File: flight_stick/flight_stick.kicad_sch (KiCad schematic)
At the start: 80 parts, among them J1 Load Cell 1, J10 USB_C_Receptacle_USB2.0, J11 Conn_01x05_Pin, J2 Load Cell 2, J3 Load Cell 5, J4 Load Cell 6, J5 Load Cell 3, J6 Load Cell 4, J7 Conn_01x04_Male, J8 Conn_01x05_Pin, J9 Conn_01x04_Male, Q1 MMS8550, Q2 MMS8550, Q3 MMS8550, Q4 2N7002, Q5 2N7002, Q6 2N7002, Q7 2N7002, Q8 2N7002, SW1 SW_Push, U1 HX711, U2 HX711, U3 HX711, U4 STM32F103C8Tx, U5 AZ1117-3.3, Y1 8Mhz

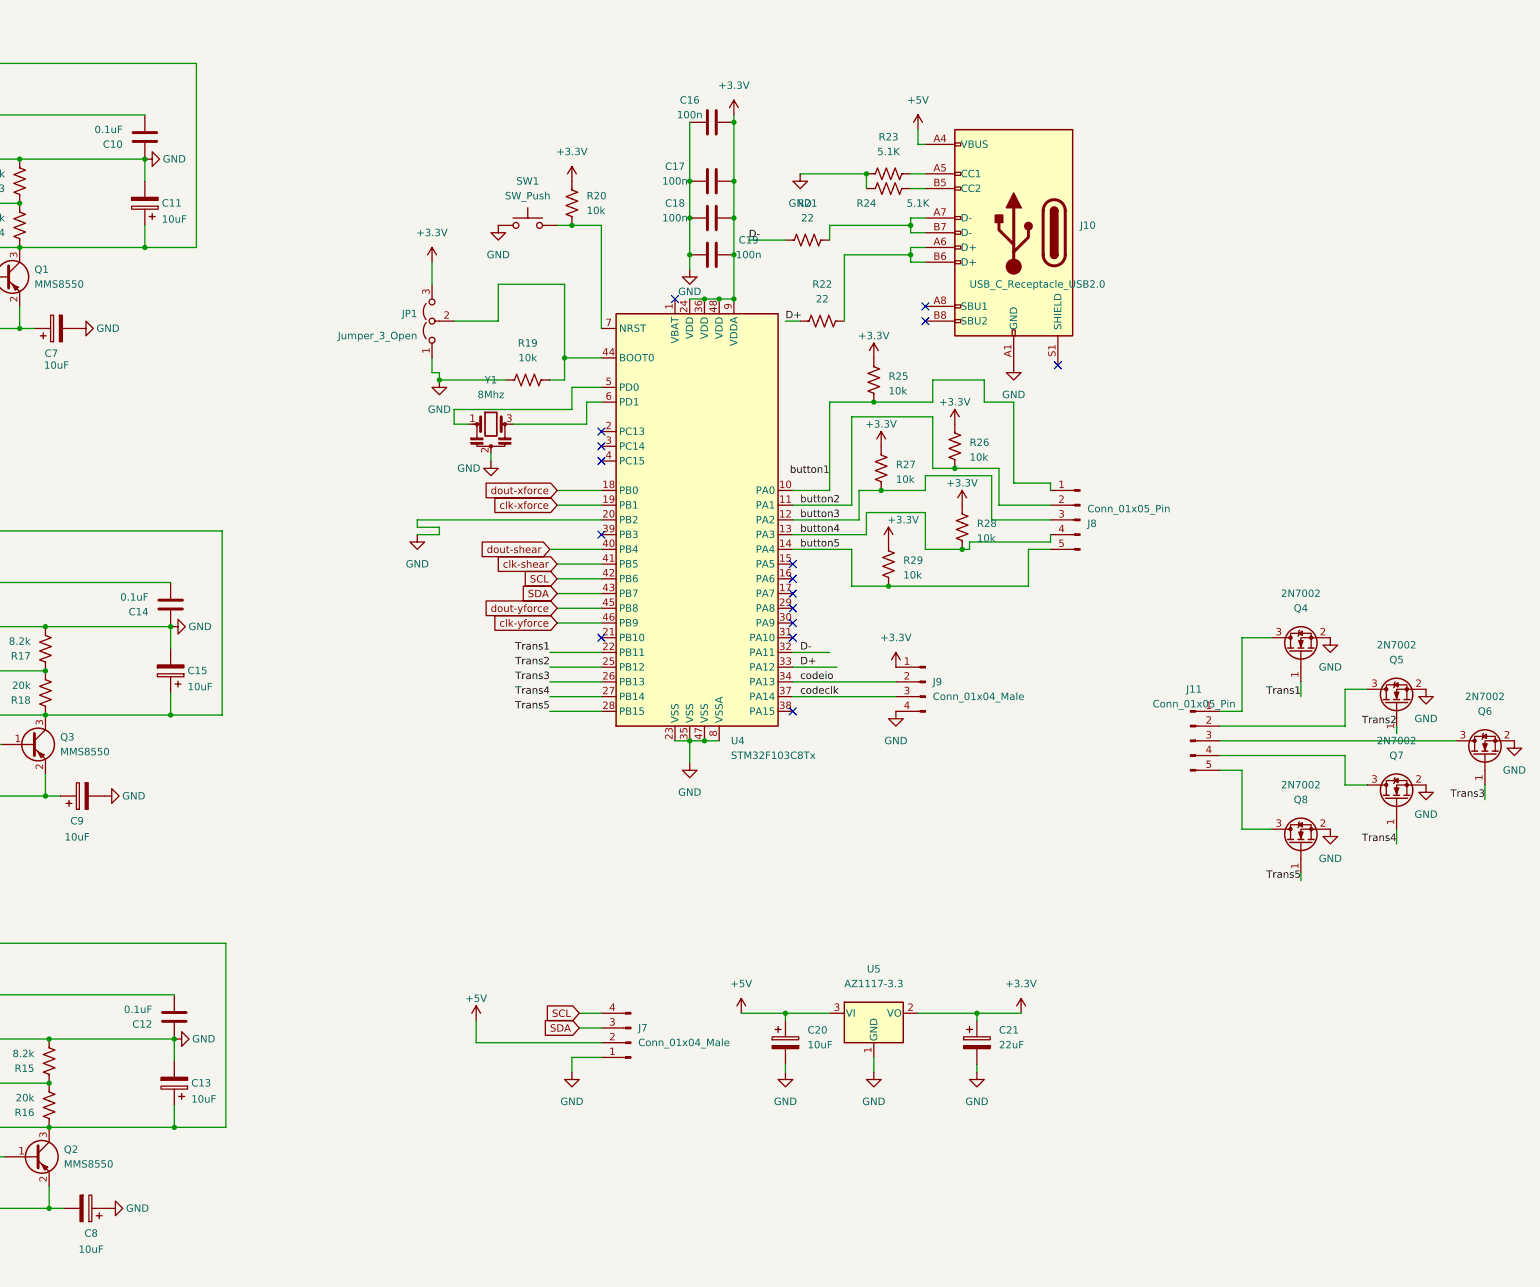
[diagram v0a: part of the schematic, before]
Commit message: Added extra LEDs, replaced Voltage reg., added redundant SW, reviewed USB placement
Added many new features
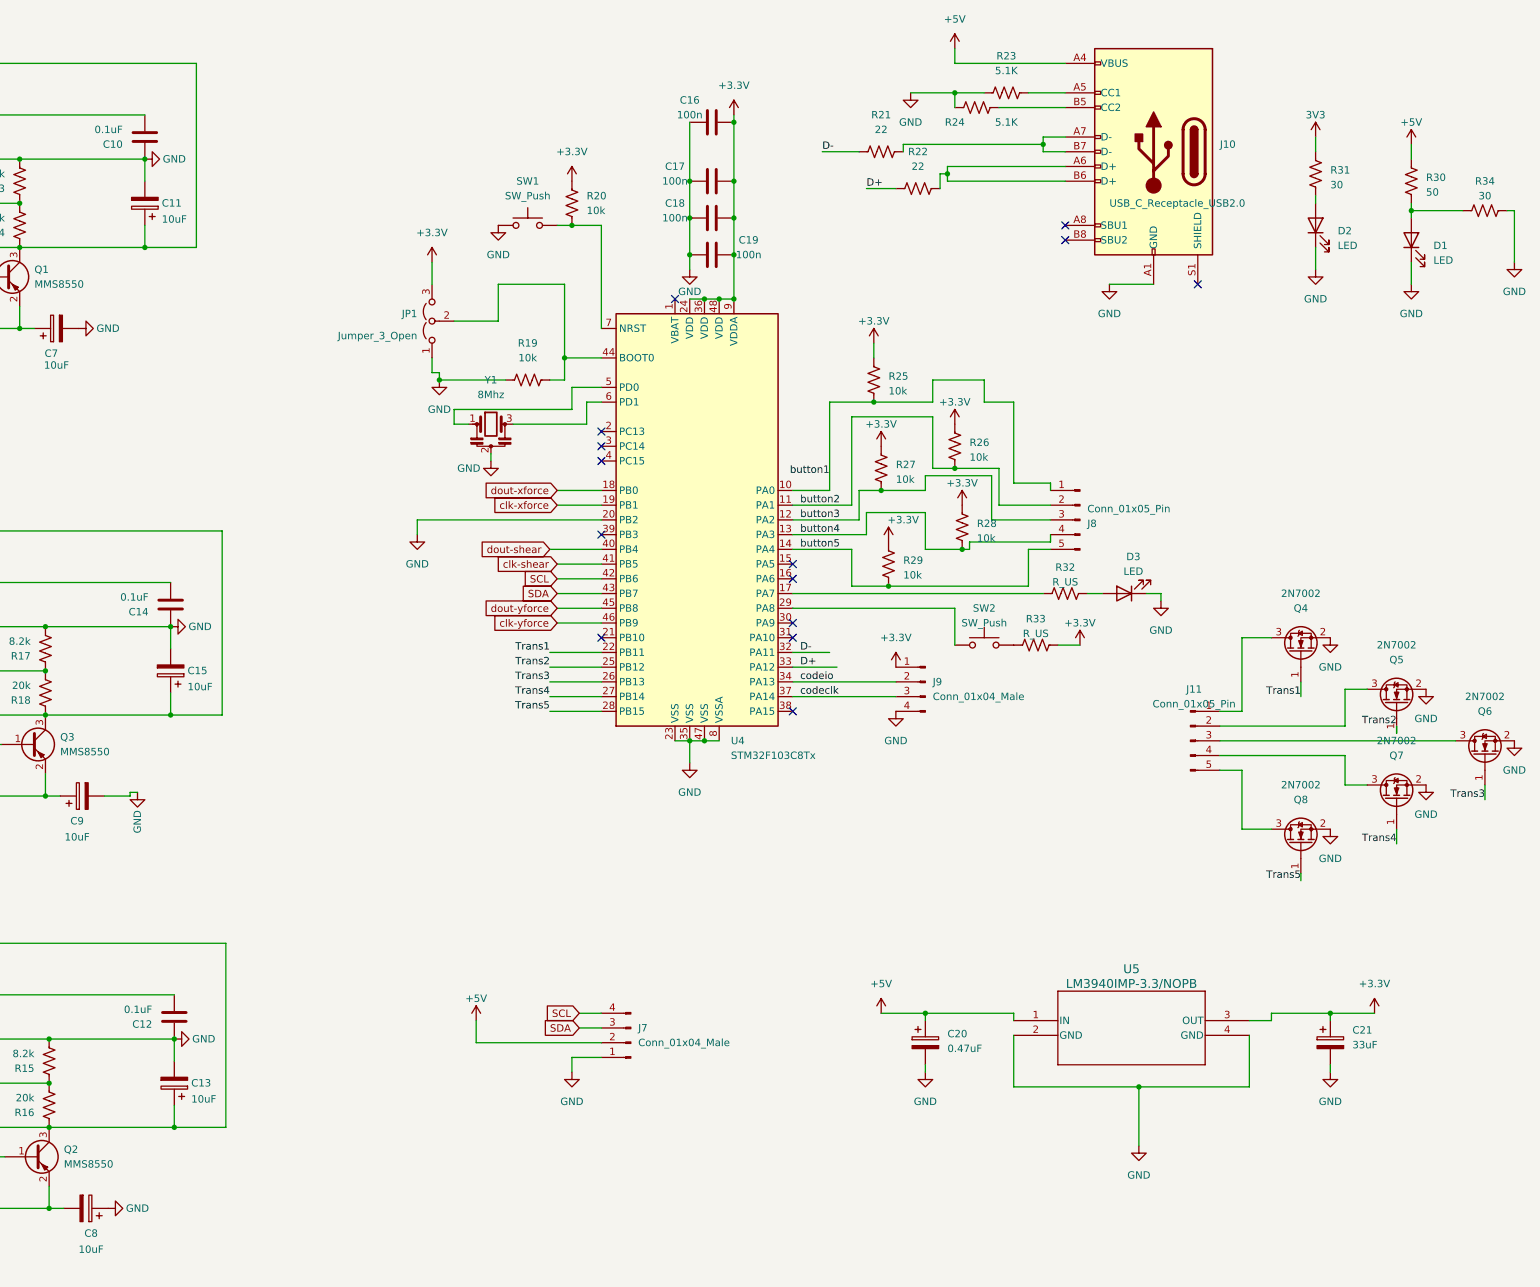
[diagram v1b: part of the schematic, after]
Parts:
- removed U5: AZ1117-3.3, Package_TO_SOT_SMD:SOT-223-3_TabPin2, symbol Regulator_Linear:AZ1117-3.3
- added D1, D2, D3: LED, LED_SMD:LED_2010_5025Metric, symbol Device:LED
- added R30: 50, Resistor_SMD:R_0603_1608Metric, symbol Device:R_US
- added R31: 30, Resistor_SMD:R_0603_1608Metric, symbol Device:R_US
- added R32, R33: R_US, Resistor_SMD:R_0603_1608Metric, symbol Device:R_US
- added R34: 30, symbol Device:R_US
- added SW2: SW_Push, symbol Switch:SW_Push
- added U5: LM3940IMP-3.3/NOPB, MP04A, symbol 2024-03-22_01-04-52:LM3940IMP-3.3_NOPB
- C20: value 10uF -> 0.47uF
- C21: value 22uF -> 33uF
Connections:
- net +3.3V: now also R33.2, U5.3 (OUT)
- net +5V: now also R30.1, R31.1, U5.1 (IN)
- net GND: now also D1.1 (K), D2.1 (K), D3.1 (K), R34.2, U5.2 (GND), U5.4 (GND)
- net at U4.17 (PA7): now also R32.1
- net at U4.29 (PA8): now also SW2.1
- new net: R33.1, SW2.2
- new net: D1.2 (A), R30.2, R34.1
- new net: D3.2 (A), R32.2
- new net: D2.2 (A), R31.2
- no-connect marks 19 -> 17
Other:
- moved on the sheet: C20, C21, J10, R21, R22, R23, R24

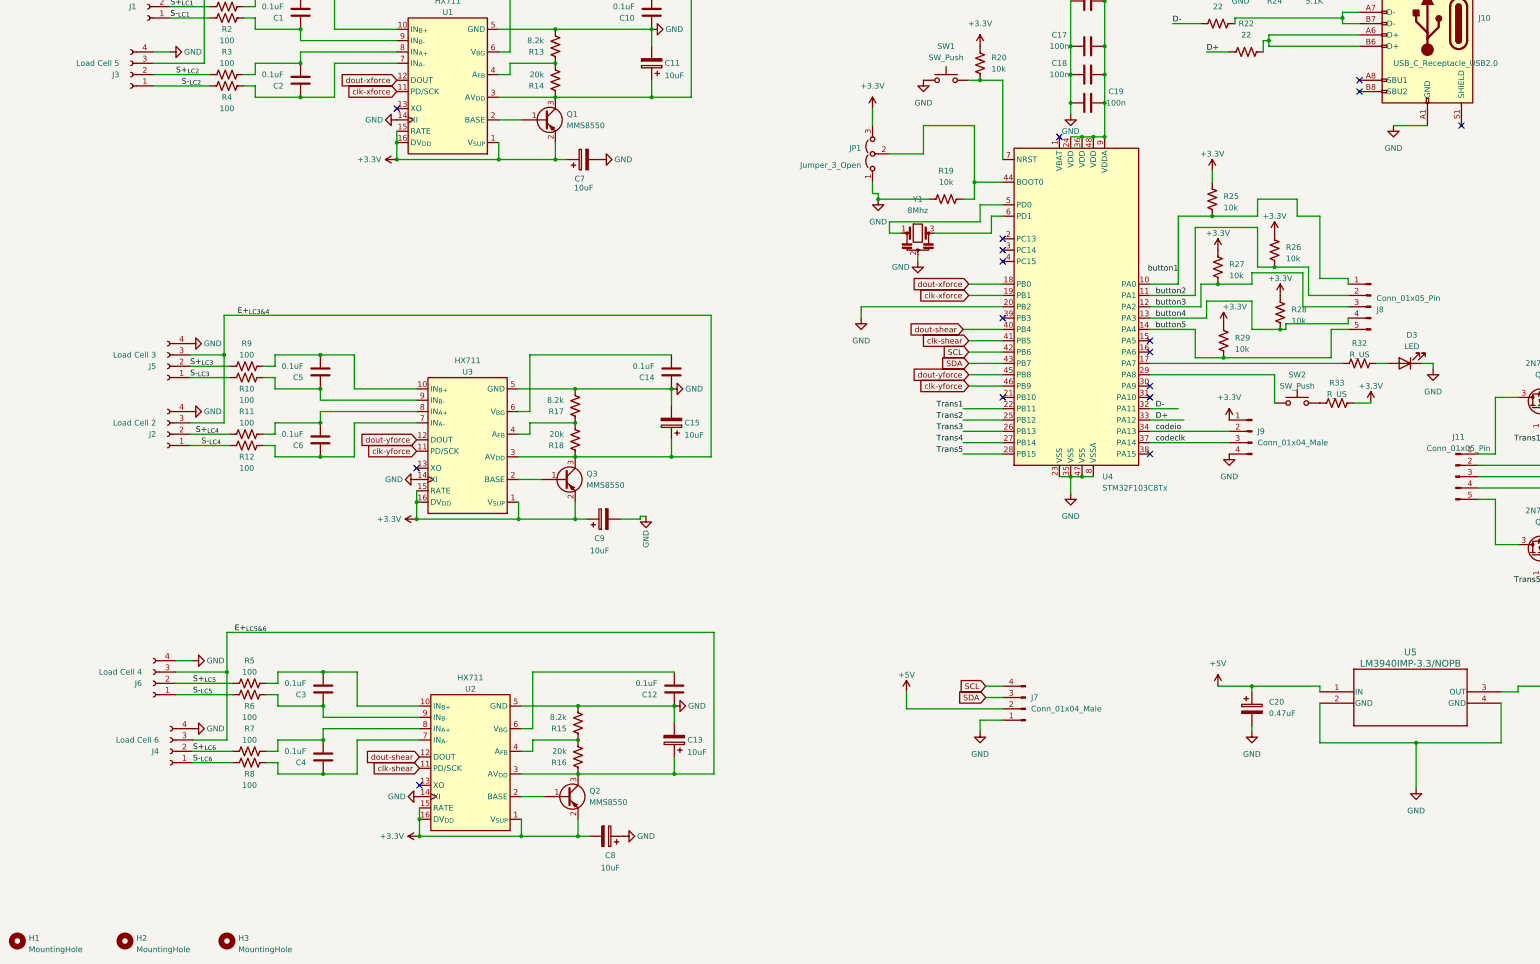
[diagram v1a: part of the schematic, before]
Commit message: updated 3rd revision
reduced the number of strain gauges and updated the schematic and placed the initial layout without traces.
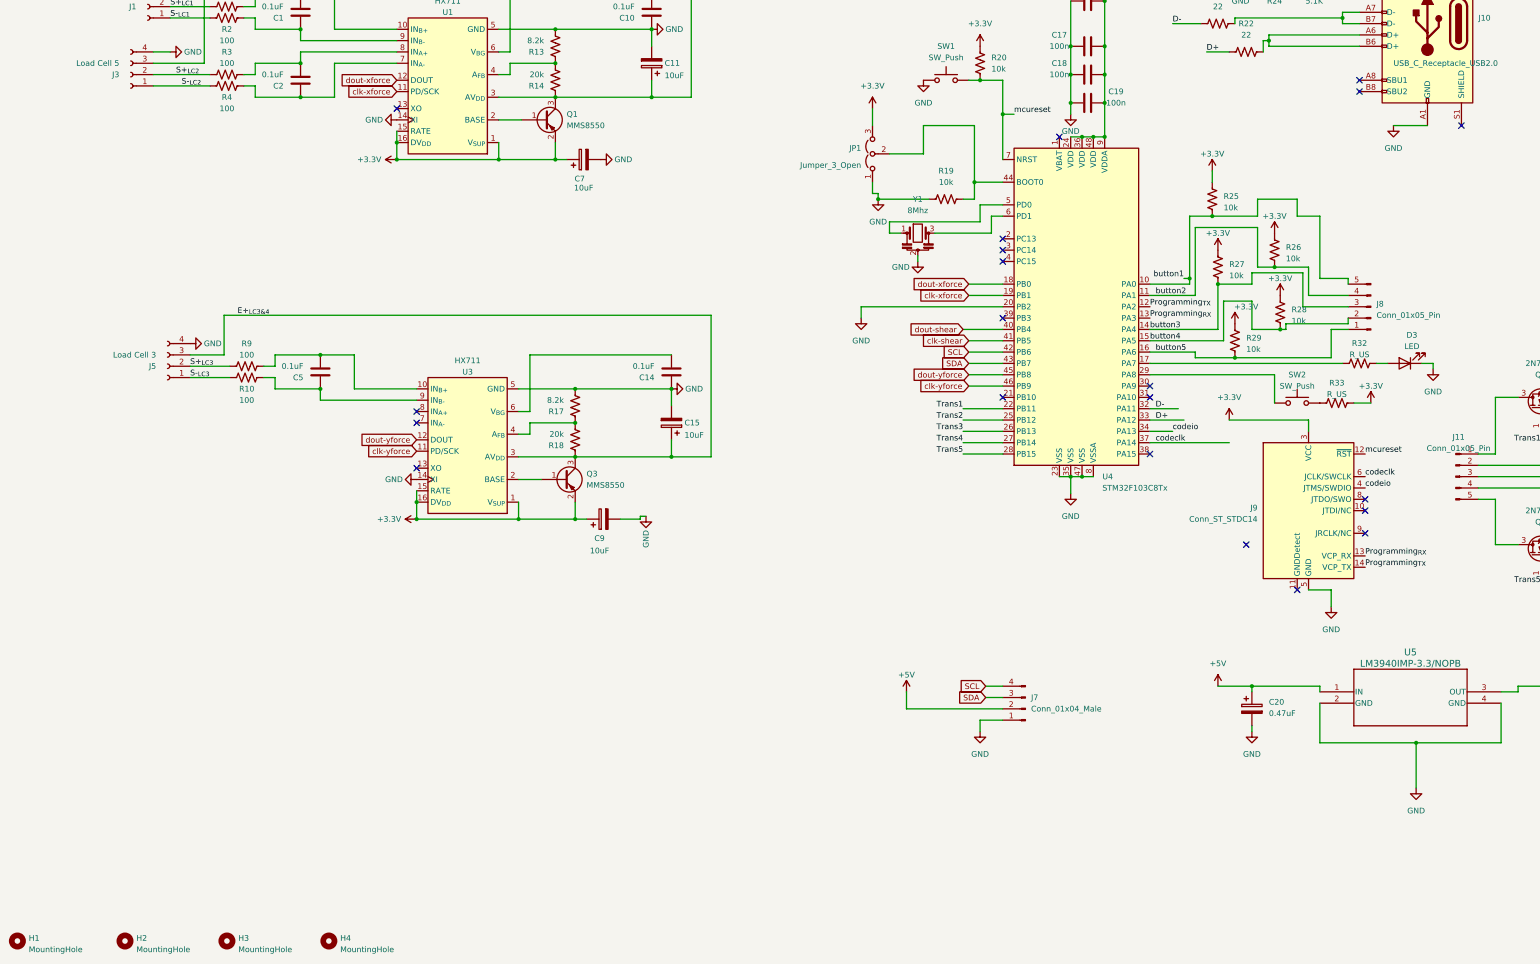
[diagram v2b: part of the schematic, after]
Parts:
- removed C12, C3, C4, C6: 0.1uF, Capacitor_SMD:C_0603_1608Metric, symbol Device:C
- removed C13, C8: 10uF, Capacitor_SMD:C_0603_1608Metric, symbol Device:C_Polarized
- removed J2: Load Cell 2, Connector_PinHeader_2.54mm:PinHeader_1x04_P2.54mm_Vertical, symbol Connector:Conn_01x04_Female
- removed J4: Load Cell 6, Connector_PinHeader_2.54mm:PinHeader_1x04_P2.54mm_Vertical, symbol Connector:Conn_01x04_Female
- removed J6: Load Cell 4, Connector_PinHeader_2.54mm:PinHeader_1x04_P2.54mm_Vertical, symbol Connector:Conn_01x04_Female
- removed J9: Conn_01x04_Male, Connector_PinHeader_2.54mm:PinHeader_1x04_P2.54mm_Horizontal, symbol Connector:Conn_01x04_Male
- removed Q2: MMS8550, Package_TO_SOT_SMD:SOT-23, symbol Device:Q_PNP_BEC
- removed R11, R12, R5, R6, R7, R8: 100, Resistor_SMD:R_0603_1608Metric, symbol Device:R_US
- removed R15: 8.2k, Resistor_SMD:R_0603_1608Metric, symbol Device:R_US
- removed R16: 20k, Resistor_SMD:R_0603_1608Metric, symbol Device:R_US
- removed U2: HX711, Package_SO:SOIC-16_3.9x9.9mm_P1.27mm, symbol wing_test:HX711
- added H4: MountingHole, MountingHole:MountingHole_3.2mm_M3_ISO7380, symbol Mechanical:MountingHole
- added J9: Conn_ST_STDC14, Connector_PinHeader_1.27mm:PinHeader_2x07_P1.27mm_Vertical_SMD, symbol Connector:Conn_ST_STDC14
- J1, J3, J5: footprint Connector_PinHeader_2.54mm:PinHeader_1x04_P2.54mm_Vertical -> Connector_PinHeader_1.00mm:PinHeader_1x04_P1.00mm_Vertical
- J7: footprint Connector_PinHeader_2.54mm:PinHeader_1x04_P2.54mm_Horizontal -> Connector_JST:JST_XH_B4B-XH-A_1x04_P2.50mm_Vertical
- R34: footprint (none) -> Resistor_SMD:R_0603_1608Metric
- SW2: footprint (none) -> Button_Switch_SMD:SW_SPST_B3U-1000P-B
- U5: footprint MP04A -> Package_TO_SOT_SMD:SOT-223
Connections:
- net +3.3V: now also J9.3 (VCC)
- net GND: now also J9.5 (GND), J9.7 (GND)
- net button1: now also J8.5 (Pin_5); no longer J8.1 (Pin_1)
- net button2: now also J8.4 (Pin_4); no longer J8.2 (Pin_2)
- net button3: now also U4.14 (PA4); no longer U4.12 (PA2)
- net button4: now also J8.2 (Pin_2), U4.15 (PA5); no longer J8.4 (Pin_4), U4.13 (PA3)
- net button5: now also J8.1 (Pin_1), U4.16 (PA6); no longer J8.5 (Pin_5), U4.14 (PA4)
- net codeclk: now also J9.6 (JCLK/SWCLK)
- net codeio: now also J9.4 (JTMS/SWDIO)
- net mcureset: now reaches R20.2, SW1.2, U4.7 (NRST)
- net mcureset: now also J9.12 (~{RST})
- new net Programming_{RX}: J9.13 (VCP_RX), U4.13 (PA3)
- new net Programming_{TX}: J9.14 (VCP_TX), U4.12 (PA2)
- no-connect marks 17 -> 21
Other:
- moved on the sheet: J8, R29
